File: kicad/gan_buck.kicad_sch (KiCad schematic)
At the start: 11 parts

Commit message: The driver is now a sub-sheet of the converter, not a separate drawing
In the netlist it always was: sim/buck.cir includes models/segdrv.lib and
instantiates it twice, so every number in this project comes from a run with
the driver in the loop. The SCHEMATIC did not say so. gan_buck.kicad_sch had
HSG and LSG as net labels and a text note claiming they "come from the
segmented gate driver", and zero hierarchical sheets -- so a reviewer reading
the sheet was entitled to say the driver was not connected to anything, and
would have been right about the drawing while wrong about the simulation.

gan_segdrv.kicad_sch is now instantiated twice inside gan_buck.kicad_sch, high
side and low side, with sheet pins for VP, VN, CTRL and GATE. eeschema's
hierarchy pane shows Root -> the two drivers, and descending into either lands
on the eight slices and the clamp. The note that stood in for the connection is
replaced by what is now true.

Two things that had to be got right rather than guessed. A sheet pin's angle
must point INTO the sheet body, so left-edge pins are at 180 and right-edge at
0; reversed, the stub lands inside the box where no wire can reach it. And
every sub-sheet needs its own entry in sheet_instances or KiCad reports the
file as damaged on open.

The routing is not free choice either, and the script says why: the decoupling
branch occupies x = 120 continuously from y = 60 to y = 115, so nothing can
cross between the drivers and the gates anywhere in that band. The high-side
feed drops to y = 122, crosses there, and comes back up at x = 138.

Downstream: re-captured all three sheets; fig_novelty_circuit now rings the two
sub-sheet instances instead of the two net labels, and its converter crop is
wide and tall enough to hold them; the film's second camera move on the buck
sheet was retuned, since the half-bridge moved right and the left of the sheet
is now the driver. SPEECH-SCRIPT.md gains the answer, including that this was
only true in the netlist until tod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
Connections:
- net Gate driver - low side/GATE: now reaches Qls.2 (G)
- net Gate driver - high side/GATE: now reaches Qhs.2 (G)
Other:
- added sheet Gate driver - high side (gan_segdrv.kicad_sch)
- added sheet Gate driver - low side (gan_segdrv.kicad_sch)
- note added: "HSG / LSG are driven by the two hierarchical sheets on the left: the"
- note added: "same gan_segdrv.kicad_sch, placed twice. Descend into either to see them."
- note removed: "HSG / LSG come from the segmented gate driver (8 pull-up + 8 pull-down"
- note removed: "slices, active Miller clamp, -2 V off rail) driven by seg_gate_ctrl.v."

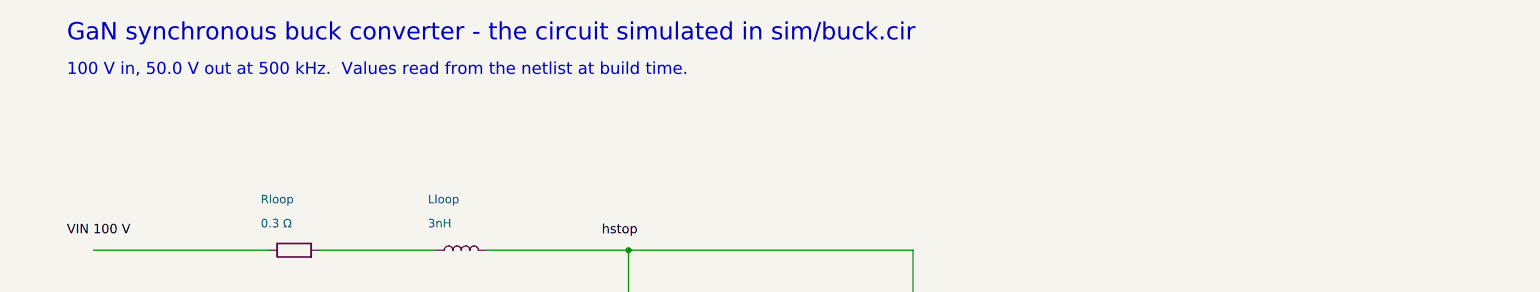
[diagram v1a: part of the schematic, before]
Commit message: Fix three figure/text contradictions the automated checks could not see
Rendering the deck and reading the figures found three places where the
picture and the words disagreed. Every guard was green throughout, because
none of them read pixels.

1. Slide 14 had the wrong figure. The caption describes two rows of
   waveforms -- the switch node over the gate it disturbs -- and was paired
   with toolout/01-ngspice-crosstalk.png, a terminal screenshot with no rows
   in it. The slide told the panel to look at a TOP and a BOTTOM that were
   not on the screen. That screenshot was also evidence against itself: it is
   dated 2026-09-08 on a MacBook running ngspice-47, while the deck states
   ngspice-42 on a Debian container. It now uses fig1_crosstalk.png, the
   figure the words were written for, and the caption names left and right
   as well as top and bottom.

2. The head-to-head chart contradicted its own title and the deck's
   headline. Its title says the base paper is re-tuned at every corner and
   the deck quotes it that way, but it plotted base_as_built: +0.34 V at the
   first corner where the text claims +0.503 V, so the slide said 5.5x while
   the bars divided to 8.1x -- in our favour. Only that one corner differs
   between the two columns, which is why three correct bars hid it.
   result_figures.py now plots base_retuned and recomputes the ratios from
   the values it is about to draw, refusing to write a chart that disagrees
   with RESULTS-SUMMARY. Reinstating the old column reproduces the refusal.

3. The converter schematic printed VIN x D -- 50.0 V, the ideal output --
   two inches above a caption saying 48.50 V. Both are right; a sheet that
   prints one while the slide prints the other reads as a mistake. It now
   prints the simulated output from the same row of results/buck_sweep.csv
   the deck quotes, and names the ideal so the 1.50 V gap is accounted for
   rather than noticed.

The schematic change flows through the KiCad captures, the t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
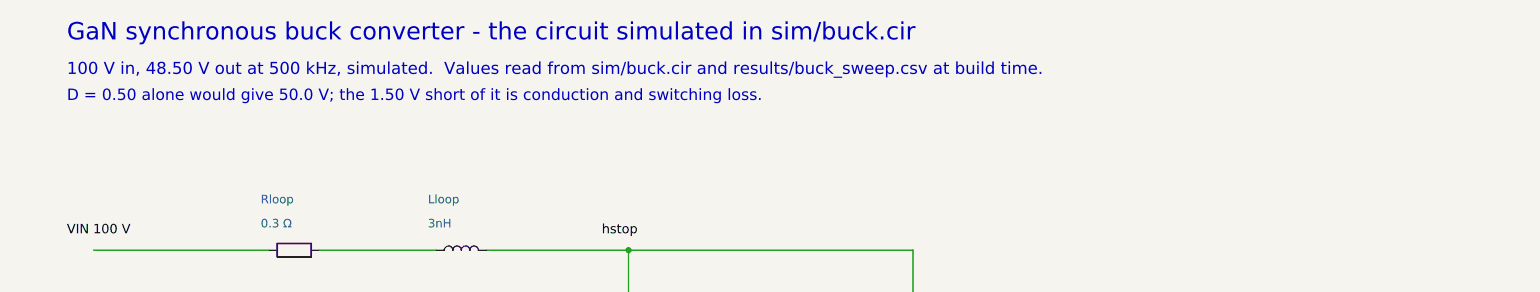
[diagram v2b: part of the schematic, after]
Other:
- note added: "100 V in, 48.50 V out at 500 kHz, simulated. Values read from sim/buck.cir and results/buck_sweep.csv at build time."
- note added: "D = 0.50 alone would give 50.0 V; the 1.50 V short of it is conduction and switching loss."
- note removed: "100 V in, 50.0 V out at 500 kHz. Values read from the netlist at build time."
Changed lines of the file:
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@@
     (property "Reference" "Rloop" (at 65.0 52.4 270) (effects (font (size 1.27 1.27)) (justify left)))
     (property "Value" "0.3 Ω" (at 65.0 56.0 270) (effects (font (size 1.27 1.27)) (justify left)))
-    (instances (project "gan_buck" (path "/1d8ec6a2-f464-4883-868c-3980009fe039" (reference "Rloop") (unit 1))))
+    (instances (project "gan_buck" (path "/22f631f6-727f-46d2-a0c6-da2fdc92410f" (reference "Rloop") (unit 1))))
   )
   (symbol (lib_id "Device:L") (at 95 60.0 90) (unit 1)
@@
     (property "Reference" "Lloop" (at 90.0 52.4 270) (effects (font (size 1.27 1.27)) (justify left)))
     (property "Value" "3nH" (at 90.0 56.0 270) (effects (font (size 1.27 1.27)) (justify left)))
-    (instances (project "gan_buck" (path "/1d8ec6a2-f464-4883-868c-3980009fe039" (reference "Lloop") (unit 1))))
+    (instances (project "gan_buck" (path "/22f631f6-727f-46d2-a0c6-da2fdc92410f" (reference "Lloop") (unit 1))))
   )
   (symbol (lib_id "Device:L") (at 120 75 0) (unit 1)
@@
     (property "Reference" "Ldec" (at 123.2 72.8 0) (effects (font (size 1.27 1.27)) (justify left)))
     (property "Value" "0.5nH" (at 123.2 76.4 0) (effects (font (size 1.27 1.27)) (justify left)))
-    (instances (project "gan_buck" (path "/1d8ec6a2-f464-4883-868c-3980009fe039" (reference "Ldec") (unit 1))))
+    (instances (project "gan_buck" (path "/22f631f6-727f-46d2-a0c6-da2fdc92410f" (reference "Ldec") (unit 1))))
   )
   (symbol (lib_id "Device:C") (at 120 90 0) (unit 1)
@@
     (property "Reference" "Cdec" (at 123.2 87.8 0) (effects (font (size 1.27 1.27)) (justify left)))
     (property "Value" "100nF" (at 123.2 91.4 0) (effects (font (size 1.27 1.27)) (justify left)))
-    (instances (project "gan_buck" (path "/1d8ec6a2-f464-4883-868c-3980009fe039" (reference "Cdec") (unit 1))))
+    (instances (project "gan_buck" (path "/22f631f6-727f-46d2-a0c6-da2fdc92410f" (reference "Cdec") (unit 1))))
   )
   (symbol (lib_id "Device:R") (at 120 105 0) (unit 1)
@@
     (property "Reference" "Rdec" (at 123.2 102.8 0) (effects (font (size 1.27 1.27)) (justify left)))
     (property "Value" "1 Ω" (at 123.2 106.4 0) (effects (font (size 1.27 1.27)) (justify left)))
-    (instances (project "gan_buck" (path "/1d8ec6a2-f464-4883-868c-3980009fe039" (reference "Rdec") (unit 1))))
+    (instances (project "gan_buck" (path "/22f631f6-727f-46d2-a0c6-da2fdc92410f" (reference "Rdec") (unit 1))))
   )
   (symbol (lib_id "power:GND") (at 120 115 0) (unit 1)
@@
     (property "Reference" "#PWR01" (at 123.2 112.8 0) (effects (font (size 1.27 1.27)) (justify left)))
     (property "Value" "GND" (at 123.2 116.4 0) (effects (font (size 1.27 1.27)) (justify left)))
-    (instances (project "gan_buck" (path "/1d8ec6a2-f464-4883-868c-3980009fe039" (reference "#PWR01") (unit 1))))
+    (instances (project "gan_buck" (path "/22f631f6-727f-46d2-a0c6-da2fdc92410f" (reference "#PWR01") (unit 1))))
   )
   (symbol (lib_id "Device:Q_NMOS_DGS") (at 160 90 0) (unit 1)
@@
     (property "Reference" "Qhs" (at 166 87.8 0) (effects (font (size 1.27 1.27)) (justify left)))
     (property "Value" "eGaN HEMT" (at 166 91.4 0) (effects (font (size 1.27 1.27)) (justify left)))
-    (instances (project "gan_buck" (path "/1d8ec6a2-f464-4883-868c-3980009fe039" (reference "Qhs") (unit 1))))
+    (instances (project "gan_buck" (path "/22f631f6-727f-46d2-a0c6-da2fdc92410f" (reference "Qhs") (unit 1))))
   )
   (symbol (lib_id "Device:Q_NMOS_DGS") (at 160 130 0) (unit 1)
@@
     (property "Reference" "Qls" (at 166 127.8 0) (effects (font (size 1.27 1.27)) (justify left)))
     (property "Value" "eGaN HEMT" (at 166 131.4 0) (effects (font (size 1.27 1.27)) (justify left)))
-    (instances (project "gan_buck" (path "/1d8ec6a2-f464-4883-868c-3980009fe039" (reference "Qls") (unit 1))))
+    (instances (project "gan_buck" (path "/22f631f6-727f-46d2-a0c6-da2fdc92410f" (reference "Qls") (unit 1))))
   )
   (symbol (lib_id "power:GND") (at 162.54 145 0) (unit 1)
@@
     (property "Reference" "#PWR02" (at 165.73999999999998 142.8 0) (effects (font (size 1.27 1.27)) (justify left)))
     (property "Value" "GND" (at 165.73999999999998 146.4 0) (effects (font (size 1.27 1.27)) (justify left)))
-    (instances (project "gan_buck" (path "/1d8ec6a2-f464-4883-868c-3980009fe039" (reference "#PWR02") (unit 1))))
+    (instances (project "gan_buck" (path "/22f631f6-727f-46d2-a0c6-da2fdc92410f" (reference "#PWR02") (unit 1))))
   )
   (sheet (at 58 76) (size 40 26)
@@
     (pin "CTRL" input (at 58 98 180) (effects (font (size 1.3 1.3)) (justify right)))
     (pin "GATE" output (at 98 89 0) (effects (font (size 1.3 1.3)) (justify left)))
-    (instances (project "gan_buck" (path "/1d8ec6a2-f464-4883-868c-3980009fe039" (page "2"))))
+    (instances (project "gan_buck" (path "/22f631f6-727f-46d2-a0c6-da2fdc92410f" (page "2"))))
   )
   (sheet (at 58 130) (size 40 26)
@@
     (pin "CTRL" input (at 58 152 180) (effects (font (size 1.3 1.3)) (justify right)))
     (pin "GATE" output (at 98 143 0) (effects (font (size 1.3 1.3)) (justify left)))
-    (instances (project "gan_buck" (path "/1d8ec6a2-f464-4883-868c-3980009fe039" (page "3"))))
+    (instances (project "gan_buck" (path "/22f631f6-727f-46d2-a0c6-da2fdc92410f" (page "3"))))
   )
   (symbol (lib_id "Device:L") (at 195 110.0 90) (unit 1)
@@
     (property "Reference" "Lo" (at 190.0 102.39999999999999 270) (effects (font (size 1.27 1.27)) (justify left)))
     (property "Value" "22uH" (at 190.0 106.0 270) (effects (font (size 1.27 1.27)) (justify left)))
-    (instances (project "gan_buck" (path "/1d8ec6a2-f464-4883-868c-3980009fe039" (reference "Lo") (unit 1))))
+    (instances (project "gan_buck" (path "/22f631f6-727f-46d2-a0c6-da2fdc92410f" (reference "Lo") (unit 1))))
   )
   (symbol (lib_id "Device:R") (at 240 120 0) (unit 1)
@@
     (property "Reference" "Resr" (at 243.2 117.8 0) (effects (font (size 1.27 1.27)) (justify left)))
     (property "Value" "0.3 Ω" (at 243.2 121.4 0) (effects (font (size 1.27 1.27)) (justify left)))
-    (instances (project "gan_buck" (path "/1d8ec6a2-f464-4883-868c-3980009fe039" (reference "Resr") (unit 1))))
+    (instances (project "gan_buck" (path "/22f631f6-727f-46d2-a0c6-da2fdc92410f" (reference "Resr") (unit 1))))
   )
   (symbol (lib_id "Device:C") (at 240 135 0) (unit 1)
@@
     (property "Reference" "Co" (at 243.2 132.8 0) (effects (font (size 1.27 1.27)) (justify left)))
     (property "Value" "4.7uF" (at 243.2 136.4 0) (effects (font (size 1.27 1.27)) (justify left)))
-    (instances (project "gan_buck" (path "/1d8ec6a2-f464-4883-868c-3980009fe039" (reference "Co") (unit 1))))
+    (instances (project "gan_buck" (path "/22f631f6-727f-46d2-a0c6-da2fdc92410f" (reference "Co") (unit 1))))
   )
   (symbol (lib_id "power:GND") (at 240 145 0) (unit 1)
@@
     (property "Reference" "#PWR03" (at 243.2 142.8 0) (effects (font (size 1.27 1.27)) (justify left)))
     (property "Value" "GND" (at 243.2 146.4 0) (effects (font (size 1.27 1.27)) (justify left)))
-    (instances (project "gan_buck" (path "/1d8ec6a2-f464-4883-868c-3980009fe039" (reference "#PWR03") (unit 1))))
+    (instances (project "gan_buck" (path "/22f631f6-727f-46d2-a0c6-da2fdc92410f" (reference "#PWR03") (unit 1))))
   )
   (symbol (lib_id "Device:R") (at 275 120 0) (unit 1)
@@
     (property "Reference" "Rload" (at 278.2 117.8 0) (effects (font (size 1.27 1.27)) (justify left)))
     (property "Value" "10 Ω" (at 278.2 121.4 0) (effects (font (size 1.27 1.27)) (justify left)))
-    (instances (project "gan_buck" (path "/1d8ec6a2-f464-4883-868c-3980009fe039" (reference "Rload") (unit 1))))
+    (instances (project "gan_buck" (path "/22f631f6-727f-46d2-a0c6-da2fdc92410f" (reference "Rload") (unit 1))))
   )
   (symbol (lib_id "power:GND") (at 275 145 0) (unit 1)
@@
     (property "Reference" "#PWR04" (at 278.2 142.8 0) (effects (font (size 1.27 1.27)) (justify left)))
     (property "Value" "GND" (at 278.2 146.4 0) (effects (font (size 1.27 1.27)) (justify left)))
-    (instances (project "gan_buck" (path "/1d8ec6a2-f464-4883-868c-3980009fe039" (reference "#PWR04") (unit 1))))
+    (instances (project "gan_buck" (path "/22f631f6-727f-46d2-a0c6-da2fdc92410f" (reference "#PWR04") (unit 1))))
   )
   (label "VIN  100 V" (at 36 58.0 0)
@@
   (text "GaN synchronous buck converter - the circuit simulated in sim/buck.cir" (at 36 26 0)
     (effects (font (size 2.6 2.6)) (justify left top)))
-  (text "100 V in, 50.0 V out at 500 kHz.  Values read from the netlist at build time." (at 36 32 0)
+  (text "100 V in, 48.50 V out at 500 kHz, simulated.  Values read from sim/buck.cir and results/buck_sweep.csv at build time." (at 36 32 0)
     (effects (font (size 1.8 1.8)) (justify left top)))
+  (text "D = 0.50 alone would give 50.0 V; the 1.50 V short of it is conduction and switching loss." (at 36 36 0)
+    (effects (font (size 1.7 1.7)) (justify left top)))
   (text "Qhs / Qls are enhancement-mode GaN HEMTs. KiCad has no GaN symbol, so an" (at 36 160 0)
     (effects (font (size 1.7 1.7)) (justify left top)))
@@
     (effects (font (size 1.7 1.7)) (justify left top)))
   (sheet_instances (path "/" (page "1"))
-    (path "/1d8ec6a2-f464-4883-868c-3980009fe039" (page "2"))
-    (path "/1d8ec6a2-f464-4883-868c-3980009fe039" (page "3")))
+    (path "/22f631f6-727f-46d2-a0c6-da2fdc92410f" (page "2"))
+    (path "/22f631f6-727f-46d2-a0c6-da2fdc92410f" (page "3")))
 )
